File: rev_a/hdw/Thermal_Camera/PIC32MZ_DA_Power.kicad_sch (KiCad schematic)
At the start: 73 parts

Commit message: lots of schematic progress
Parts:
- C? (x31): footprint Capacitors_SMD:C_0603 -> (none); Digi-Key PN 1276-1935-1-ND -> (none); display_footprint 0603 -> (none)
- C? (x31): footprint Capacitors_SMD:C_0603 -> (none); display_footprint 0603 -> (none)
- C? (x2): footprint Capacitors_SMD:C_0603 -> (none); Digi-Key PN 13-CC0603JPNPO9BN470CT-ND -> (none); display_footprint 0603 -> (none)
- L? (x2): footprint Inductors_SMD:L_0603 -> (none); Digi-Key PN 490-1014-1-ND -> (none)
- R? (x2): footprint Resistors_SMD:R_0603 -> (none); Wattage 1/10W -> (none); display_footprint 0603 -> (none)
- R? (x2): footprint Resistors_SMD:R_0603 -> (none); Digi-Key PN 541-5306-1-ND -> (none); Wattage 1/10W -> (none); display_footprint 0603 -> (none)
- gave numbers to parts that had none: 3
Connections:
- no-connect marks 0 -> 1

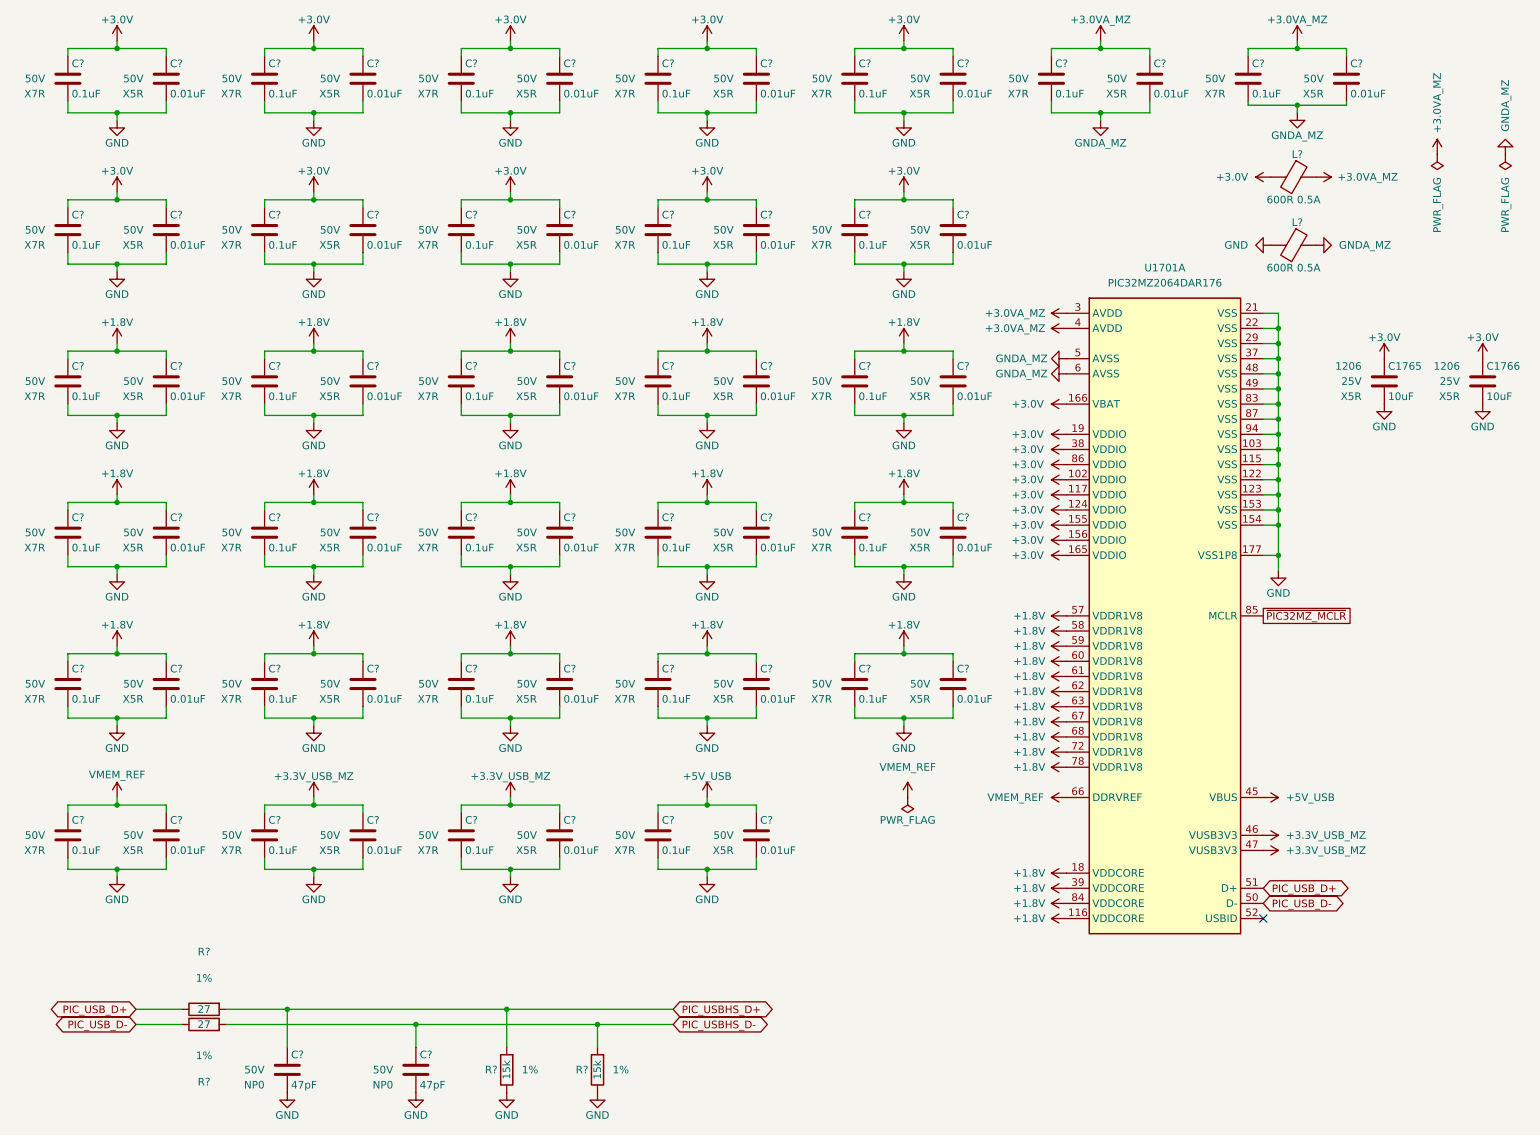
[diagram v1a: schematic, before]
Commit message: assigned a ton of footprints
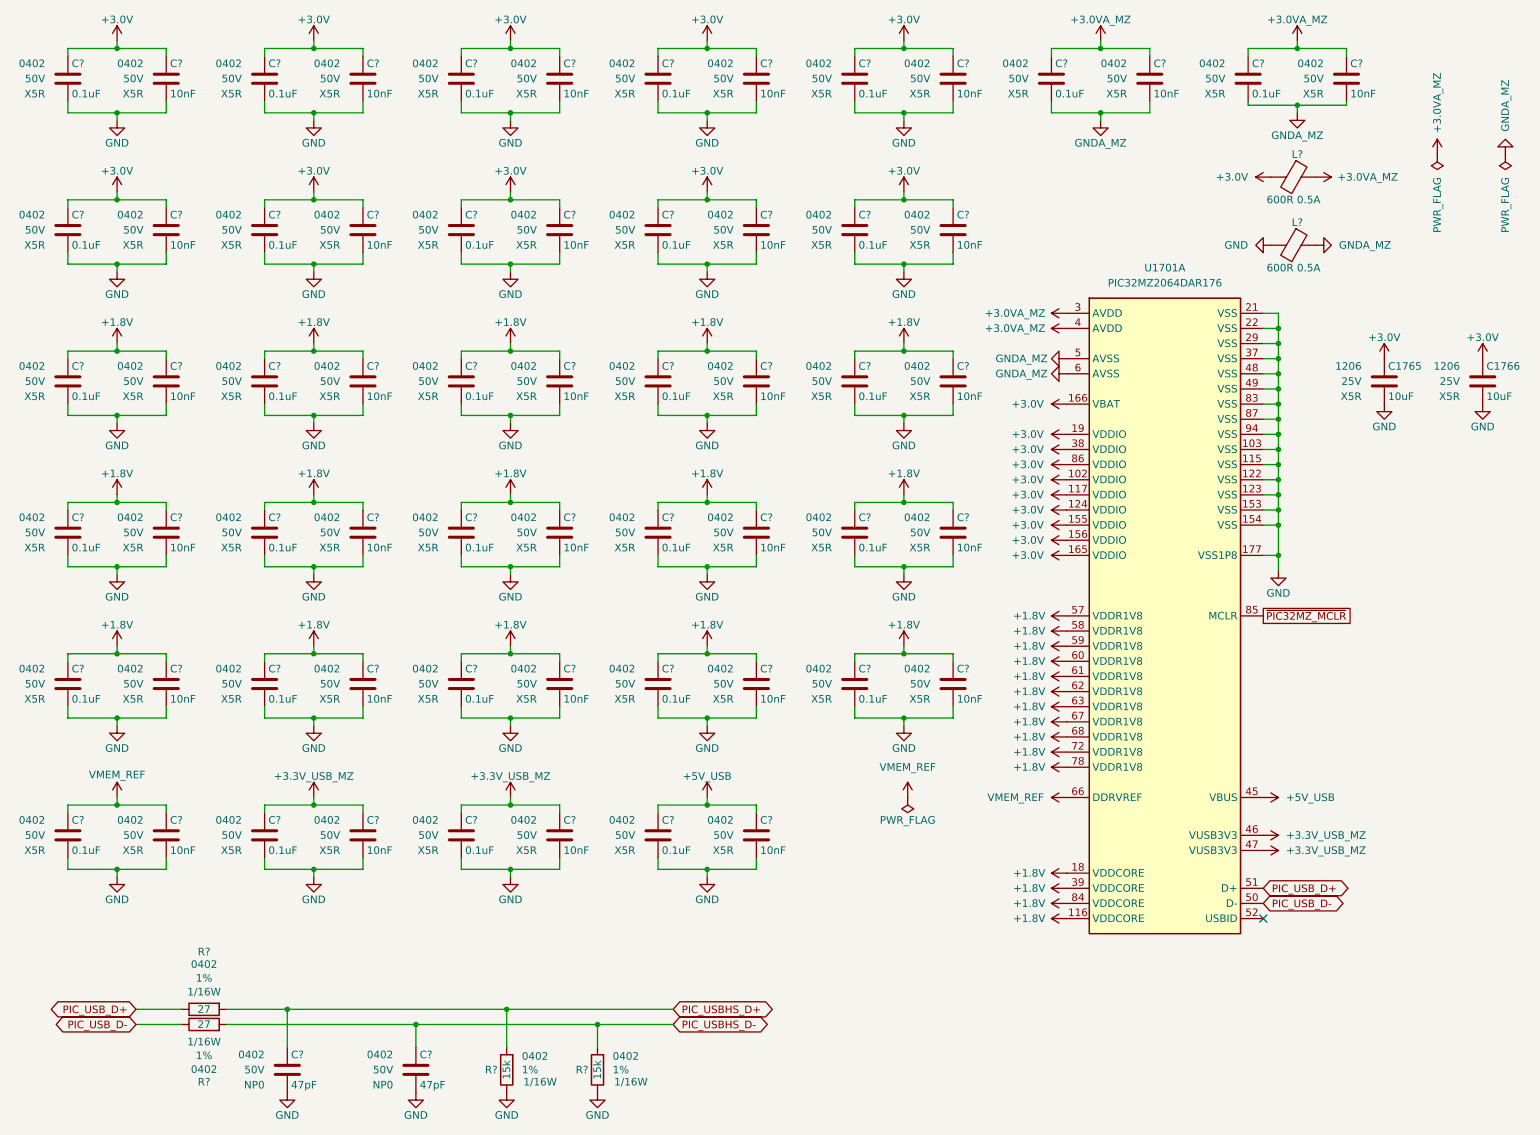
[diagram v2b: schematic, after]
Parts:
- C? (x31): footprint (none) -> Capacitors_SMD:C_0402; Dielectric X7R -> X5R; display_footprint (none) -> 0402
- C? (x31): value 0.01uF -> 10nF; footprint (none) -> Capacitors_SMD:C_0402; display_footprint (none) -> 0402
- C? (x2): footprint (none) -> Capacitors_SMD:C_0402; display_footprint (none) -> 0402
- L? (x2): footprint (none) -> Inductors_SMD:L_0402
- R? (x4): footprint (none) -> Resistors_SMD:R_0402; Wattage (none) -> 1/16W; display_footprint (none) -> 0402

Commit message: assigned some part numbers
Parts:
- C? (x31): Digi-Key PN (none) -> 490-10697-1-ND
- C? (x31): Digi-Key PN (none) -> 445-12201-1-ND
- C? (x2): Digi-Key PN (none) -> 490-5942-1-ND
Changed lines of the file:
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@@
 			)
 		)
-		(property "Digi-Key PN" ""
+		(property "Digi-Key PN" "490-10697-1-ND"
 			(at -77.724 250.952 0)
 			(effects
@@
 			)
 		)
-		(property "Digi-Key PN" ""
+		(property "Digi-Key PN" "445-12201-1-ND"
 			(at 137.16 152.4 0)
 			(effects
@@
 			)
 		)
-		(property "Digi-Key PN" ""
+		(property "Digi-Key PN" "490-10697-1-ND"
 			(at -44.704 225.552 0)
 			(effects
@@
 			)
 		)
-		(property "Digi-Key PN" ""
+		(property "Digi-Key PN" "490-10697-1-ND"
 			(at -77.724 200.152 0)
 			(effects
@@
 			)
 		)
-		(property "Digi-Key PN" ""
+		(property "Digi-Key PN" "490-10697-1-ND"
 			(at 21.336 200.152 0)
 			(effects
@@
 			)
 		)
-		(property "Digi-Key PN" ""
+		(property "Digi-Key PN" "490-10697-1-ND"
 			(at -44.704 301.752 0)
 			(effects
@@
 			)
 		)
-		(property "Digi-Key PN" ""
+		(property "Digi-Key PN" "445-12201-1-ND"
 			(at 104.14 50.8 0)
 			(effects
@@
 			)
 		)
-		(property "Digi-Key PN" ""
+		(property "Digi-Key PN" "490-10697-1-ND"
 			(at -11.684 276.352 0)
 			(effects
@@
 			)
 		)
-		(property "Digi-Key PN" ""
+		(property "Digi-Key PN" "445-12201-1-ND"
 			(at 137.16 76.2 0)
 			(effects
@@
 			)
 		)
-		(property "Digi-Key PN" ""
+		(property "Digi-Key PN" "445-12201-1-ND"
 			(at 104.14 101.6 0)
 			(effects
@@
 			)
 		)
-		(property "Digi-Key PN" ""
+		(property "Digi-Key PN" "490-10697-1-ND"
 			(at -11.684 225.552 0)
 			(effects
@@
 			)
 		)
-		(property "Digi-Key PN" ""
+		(property "Digi-Key PN" "445-12201-1-ND"
 			(at 170.18 50.8 0)
 			(effects
@@
 			)
 		)
-		(property "Digi-Key PN" ""
+		(property "Digi-Key PN" "445-12201-1-ND"
 			(at 137.16 50.8 0)
 			(effects
@@
 			)
 		)
-		(property "Digi-Key PN" ""
+		(property "Digi-Key PN" "445-12201-1-ND"
 			(at 170.18 101.6 0)
 			(effects
@@
 			)
 		)
-		(property "Digi-Key PN" ""
+		(property "Digi-Key PN" "445-12201-1-ND"
 			(at 71.12 152.4 0)
 			(effects
@@
 			)
 		)
-		(property "Digi-Key PN" ""
+		(property "Digi-Key PN" "445-12201-1-ND"
 			(at 38.1 50.8 0)
 			(effects
@@
 			)
 		)
-		(property "Digi-Key PN" ""
+		(property "Digi-Key PN" "490-10697-1-ND"
 			(at -11.684 250.952 0)
 			(effects
@@
 			)
 		)
-		(property "Digi-Key PN" ""
+		(property "Digi-Key PN" "490-10697-1-ND"
 			(at 21.336 225.552 0)
 			(effects
@@
 			)
 		)
-		(property "Digi-Key PN" ""
+		(property "Digi-Key PN" "445-12201-1-ND"
 			(at 104.14 127 0)
 			(effects
@@
 			)
 		)
-		(property "Digi-Key PN" ""
+		(property "Digi-Key PN" "490-10697-1-ND"
 			(at 54.356 200.152 0)
 			(effects
@@
 			)
 		)
-		(property "Digi-Key PN" ""
+		(property "Digi-Key PN" "490-10697-1-ND"
 			(at 87.376 200.152 0)
 			(effects
@@
 			)
 		)
-		(property "Digi-Key PN" ""
+		(property "Digi-Key PN" "490-10697-1-ND"
 			(at 21.336 301.752 0)
 			(effects
@@
 			)
 		)
-		(property "Digi-Key PN" ""
+		(property "Digi-Key PN" "445-12201-1-ND"
 			(at 38.1 25.4 0)
 			(effects
@@
 			)
 		)
-		(property "Digi-Key PN" ""
+		(property "Digi-Key PN" "445-12201-1-ND"
 			(at 170.18 25.4 0)
 			(effects
@@
 			)
 		)
-		(property "Digi-Key PN" ""
+		(property "Digi-Key PN" "445-12201-1-ND"
 			(at 38.1 152.4 0)
 			(effects
@@
 			)
 		)
-		(property "Digi-Key PN" ""
+		(property "Digi-Key PN" "445-12201-1-ND"
 			(at 38.1 101.6 0)
 			(effects
@@
 			)
 		)
-		(property "Digi-Key PN" ""
+		(property "Digi-Key PN" "490-10697-1-ND"
 			(at -44.704 276.352 0)
 			(effects
@@
 			)
 		)
-		(property "Digi-Key PN" ""
+		(property "Digi-Key PN" "445-12201-1-ND"
 			(at 38.1 76.2 0)
 			(effects
@@
 			)
 		)
-		(property "Digi-Key PN" ""
+		(property "Digi-Key PN" "490-10697-1-ND"
 			(at 21.336 250.952 0)
 			(effects
@@
 			)
 		)
-		(property "Digi-Key PN" ""
+		(property "Digi-Key PN" "445-12201-1-ND"
 			(at 137.16 25.4 0)
 			(effects
@@
 			)
 		)
-		(property "Digi-Key PN" ""
+		(property "Digi-Key PN" "490-10697-1-ND"
 			(at -11.684 301.752 0)
 			(effects
@@
 			)
 		)
-		(property "Digi-Key PN" ""
+		(property "Digi-Key PN" "490-10697-1-ND"
 			(at -11.684 200.152 0)
 			(effects
@@
 			)
 		)
-		(property "Digi-Key PN" ""
+		(property "Digi-Key PN" "490-10697-1-ND"
 			(at -44.704 200.152 0)
 			(effects
@@
 			)
 		)
-		(property "Digi-Key PN" ""
+		(property "Digi-Key PN" "445-12201-1-ND"
 			(at 137.16 101.6 0)
 			(effects
@@
 			)
 		)
-		(property "Digi-Key PN" ""
+		(property "Digi-Key PN" "445-12201-1-ND"
 			(at 71.12 101.6 0)
 			(effects
@@
 			)
 		)
-		(property "Digi-Key PN" ""
+		(property "Digi-Key PN" "490-10697-1-ND"
 			(at 120.396 200.152 0)
 			(effects
@@
 			)
 		)
-		(property "Digi-Key PN" ""
+		(property "Digi-Key PN" "490-10697-1-ND"
 			(at 21.336 327.152 0)
 			(effects
@@
 			)
 		)
-		(property "Digi-Key PN" ""
+		(property "Digi-Key PN" "445-12201-1-ND"
 			(at 236.22 25.4 0)
 			(effects
@@
 			)
 		)
-		(property "Digi-Key PN" ""
+		(property "Digi-Key PN" "490-10697-1-ND"
 			(at 54.356 250.952 0)
 			(effects
@@
 			)
 		)
-		(property "Digi-Key PN" ""
+		(property "Digi-Key PN" "490-5942-1-ND"
 			(at 58.42 191.77 0)
 			(effects
@@
 			)
 		)
-		(property "Digi-Key PN" ""
+		(property "Digi-Key PN" "445-12201-1-ND"
 			(at 104.14 76.2 0)
 			(effects
@@
 			)
 		)
-		(property "Digi-Key PN" ""
+		(property "Digi-Key PN" "445-12201-1-ND"
 			(at 71.12 127 0)
 			(effects
@@
 			)
 		)
-		(property "Digi-Key PN" ""
+		(property "Digi-Key PN" "445-12201-1-ND"
 			(at 104.14 152.4 0)
 			(effects
@@
 			)
 		)
-		(property "Digi-Key PN" ""
+		(property "Digi-Key PN" "490-10697-1-ND"
 			(at 21.336 276.352 0)
 			(effects
@@
 			)
 		)
-		(property "Digi-Key PN" ""
+		(property "Digi-Key PN" "490-10697-1-ND"
 			(at -77.724 225.552 0)
 			(effects
@@
 			)
 		)
-		(property "Digi-Key PN" ""
+		(property "Digi-Key PN" "490-10697-1-ND"
 			(at -77.724 327.152 0)
 			(effects
@@
 			)
 		)
-		(property "Digi-Key PN" ""
+		(property "Digi-Key PN" "445-12201-1-ND"
 			(at 71.12 25.4 0)
 			(effects
@@
 			)
 		)
-		(property "Digi-Key PN" ""
+		(property "Digi-Key PN" "445-12201-1-ND"
 			(at 71.12 76.2 0)
 			(effects
@@
 			)
 		)
-		(property "Digi-Key PN" ""
+		(property "Digi-Key PN" "445-12201-1-ND"
 			(at 170.18 127 0)
 			(effects
@@
 			)
 		)
-		(property "Digi-Key PN" ""
+		(property "Digi-Key PN" "490-10697-1-ND"
 			(at 54.356 276.352 0)
 			(effects
@@
 			)
 		)
-		(property "Digi-Key PN" ""
+		(property "Digi-Key PN" "445-12201-1-ND"
 			(at 71.12 50.8 0)
 			(effects
@@
 			)
 		)
-		(property "Digi-Key PN" ""
+		(property "Digi-Key PN" "490-5942-1-ND"
 			(at 80.01 191.77 0)
 			(effects
@@
 			)
 		)
-		(property "Digi-Key PN" ""
+		(property "Digi-Key PN" "490-10697-1-ND"
 			(at -44.704 327.152 0)
 			(effects
@@
 			)
 		)
-		(property "Digi-Key PN" ""
+		(property "Digi-Key PN" "445-12201-1-ND"
 			(at 170.18 76.2 0)
 			(effects
@@
 			)
 		)
-		(property "Digi-Key PN" ""
+		(property "Digi-Key PN" "490-10697-1-ND"
 			(at 54.356 225.552 0)
 			(effects
@@
 			)
 		)
-		(property "Digi-Key PN" ""
+		(property "Digi-Key PN" "445-12201-1-ND"
 			(at 38.1 127 0)
 			(effects
@@
 			)
 		)
-		(property "Digi-Key PN" ""
+		(property "Digi-Key PN" "490-10697-1-ND"
 			(at -77.724 276.352 0)
 			(effects
@@
 			)
 		)
-		(property "Digi-Key PN" ""
+		(property "Digi-Key PN" "490-10697-1-ND"
 			(at -44.704 250.952 0)
 			(effects
@@
 			)
 		)
-		(property "Digi-Key PN" ""
+		(property "Digi-Key PN" "445-12201-1-ND"
 			(at 104.14 25.4 0)
 			(effects
@@
 			)
 		)
-		(property "Digi-Key PN" ""
+		(property "Digi-Key PN" "490-10697-1-ND"
 			(at -77.724 301.752 0)
 			(effects
@@
 			)
 		)
-		(property "Digi-Key PN" ""
+		(property "Digi-Key PN" "445-12201-1-ND"
 			(at 203.2 25.4 0)
 			(effects
@@
 			)
 		)
-		(property "Digi-Key PN" ""
+		(property "Digi-Key PN" "445-12201-1-ND"
 			(at 137.16 127 0)
 			(effects
@@
 			)
 		)
-		(property "Digi-Key PN" ""
+		(property "Digi-Key PN" "490-10697-1-ND"
 			(at 54.356 301.752 0)
 			(effects
@@
 			)
 		)
-		(property "Digi-Key PN" ""
+		(property "Digi-Key PN" "490-10697-1-ND"
 			(at -11.684 327.152 0)
 			(effects

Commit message: assigned resistor part numbers
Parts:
- R? (x2): Digi-Key PN (none) -> RMCF0402FT15K0CT-ND
- R? (x2): Digi-Key PN (none) -> RMCF0402FT27R0CT-ND
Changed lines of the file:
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@@
 			)
 		)
-		(property "Digi-Key PN" ""
+		(property "Digi-Key PN" "RMCF0402FT15K0CT-ND"
 			(at 118.11 181.61 0)
 			(effects
@@
 			)
 		)
-		(property "Digi-Key PN" ""
+		(property "Digi-Key PN" "RMCF0402FT15K0CT-ND"
 			(at 102.87 181.61 0)
 			(effects
@@
 			)
 		)
-		(property "Digi-Key PN" ""
+		(property "Digi-Key PN" "RMCF0402FT27R0CT-ND"
 			(at 54.61 191.77 0)
 			(effects
@@
 			)
 		)
-		(property "Digi-Key PN" ""
+		(property "Digi-Key PN" "RMCF0402FT27R0CT-ND"
 			(at 54.61 173.99 0)
 			(effects
